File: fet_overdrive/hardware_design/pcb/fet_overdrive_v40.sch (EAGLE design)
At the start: 38 parts, among them IC1 TL072CD, J1 PJ301_THONKICONN6, J2 PJ301_THONKICONN6, Q1 MMBFJ111, Q2 SMMBT3904LT1G

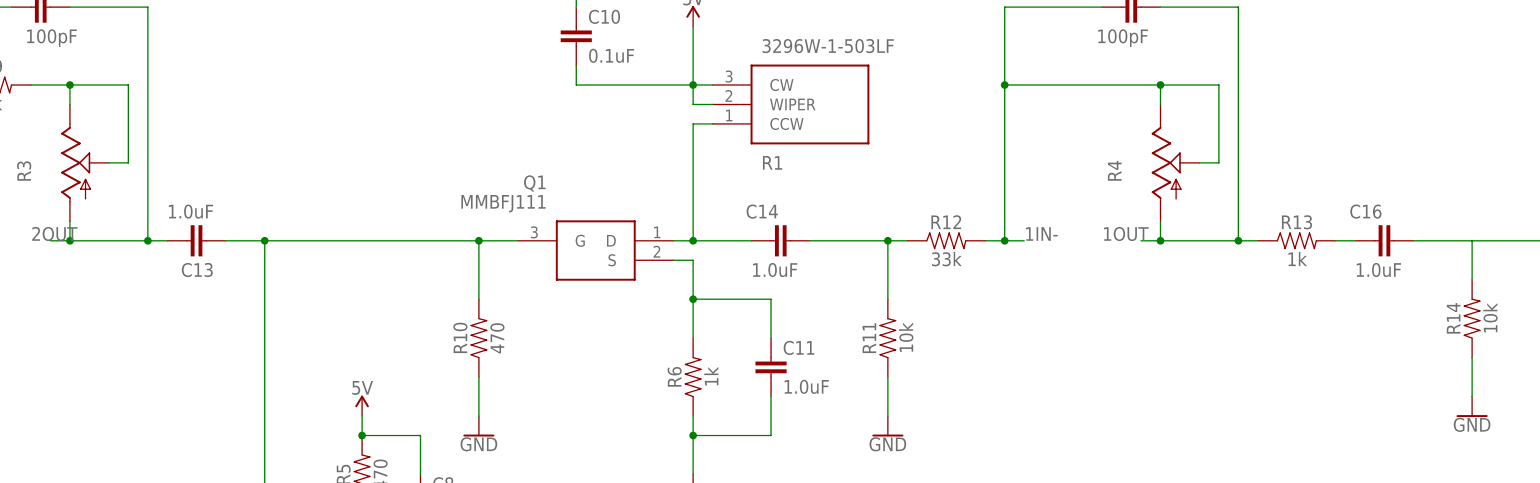
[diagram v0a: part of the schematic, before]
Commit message: changed 1uF to 10uF to keep more low end in audio signal
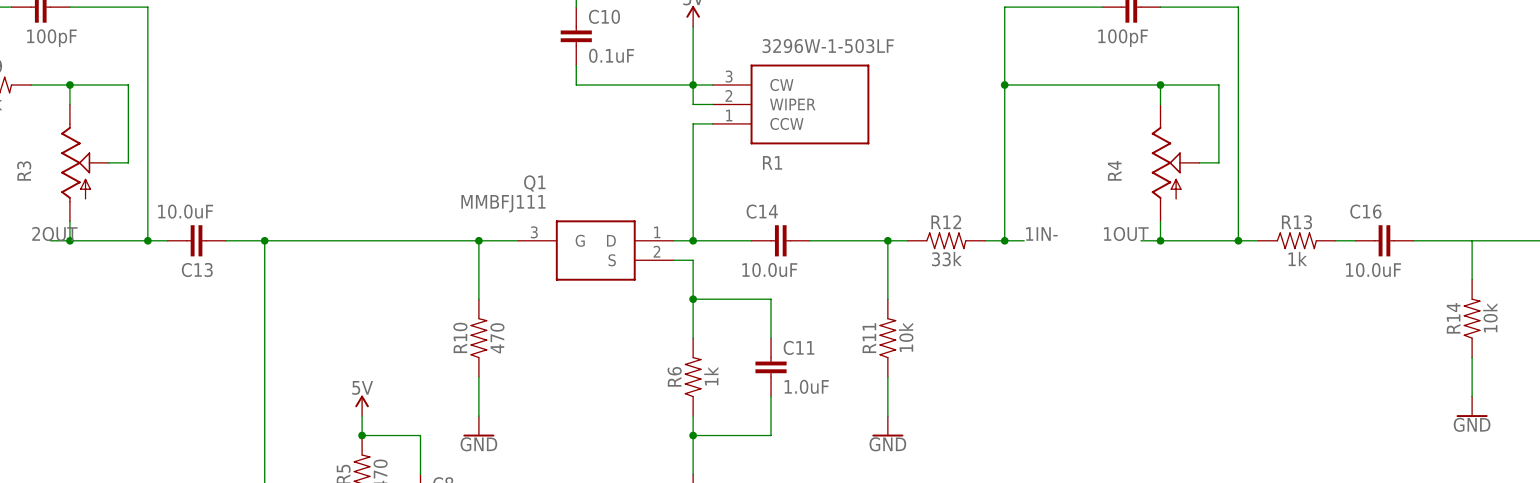
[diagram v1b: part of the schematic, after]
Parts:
- C13, C14, C16: value 1.0uF -> 10.0uF
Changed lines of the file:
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@@
 <part name="R9" library="SparkFun-Resistors" library_urn="urn:adsk.eagle:library:532" deviceset="1KOHM" device="-0603-1/10W-1%" package3d_urn="urn:adsk.eagle:package:39650/1" value="1k"/>
 <part name="C12" library="SparkFun-Capacitors" library_urn="urn:adsk.eagle:library:510" deviceset="100PF" device="-0603-50V-5%" package3d_urn="urn:adsk.eagle:package:37414/1" value="100pF"/>
-<part name="C13" library="SparkFun-Capacitors" library_urn="urn:adsk.eagle:library:510" deviceset="1.0UF" device="-0603-16V-10%" package3d_urn="urn:adsk.eagle:package:37414/1" value="1.0uF"/>
+<part name="C13" library="SparkFun-Capacitors" library_urn="urn:adsk.eagle:library:510" deviceset="1.0UF" device="-0603-16V-10%" package3d_urn="urn:adsk.eagle:package:37414/1" value="10.0uF"/>
 <part name="R10" library="SparkFun-Resistors" library_urn="urn:adsk.eagle:library:532" deviceset="470OHM" device="-0603-1/10W-1%" package3d_urn="urn:adsk.eagle:package:39650/1" value="470"/>
 <part name="GND14" library="SparkFun-PowerSymbols" library_urn="urn:adsk.eagle:library:530" deviceset="GND" device=""/>
-<part name="C14" library="SparkFun-Capacitors" library_urn="urn:adsk.eagle:library:510" deviceset="1.0UF" device="-0603-16V-10%" package3d_urn="urn:adsk.eagle:package:37414/1" value="1.0uF"/>
+<part name="C14" library="SparkFun-Capacitors" library_urn="urn:adsk.eagle:library:510" deviceset="1.0UF" device="-0603-16V-10%" package3d_urn="urn:adsk.eagle:package:37414/1" value="10.0uF"/>
 <part name="R11" library="SparkFun-Resistors" library_urn="urn:adsk.eagle:library:532" deviceset="10KOHM" device="-0603-1/10W-1%" package3d_urn="urn:adsk.eagle:package:39650/1" value="10k"/>
 <part name="GND15" library="SparkFun-PowerSymbols" library_urn="urn:adsk.eagle:library:530" deviceset="GND" device=""/>
@@
 <part name="C15" library="SparkFun-Capacitors" library_urn="urn:adsk.eagle:library:510" deviceset="100PF" device="-0603-50V-5%" package3d_urn="urn:adsk.eagle:package:37414/1" value="100pF"/>
 <part name="R13" library="SparkFun-Resistors" library_urn="urn:adsk.eagle:library:532" deviceset="1KOHM" device="-0603-1/10W-1%" package3d_urn="urn:adsk.eagle:package:39650/1" value="1k"/>
-<part name="C16" library="SparkFun-Capacitors" library_urn="urn:adsk.eagle:library:510" deviceset="1.0UF" device="-0603-16V-10%" package3d_urn="urn:adsk.eagle:package:37414/1" value="1.0uF"/>
+<part name="C16" library="SparkFun-Capacitors" library_urn="urn:adsk.eagle:library:510" deviceset="1.0UF" device="-0603-16V-10%" package3d_urn="urn:adsk.eagle:package:37414/1" value="10.0uF"/>
 <part name="R14" library="SparkFun-Resistors" library_urn="urn:adsk.eagle:library:532" deviceset="10KOHM" device="-0603-1/10W-1%" package3d_urn="urn:adsk.eagle:package:39650/1" value="10k"/>
 <part name="GND16" library="SparkFun-PowerSymbols" library_urn="urn:adsk.eagle:library:530" deviceset="GND" device=""/>
